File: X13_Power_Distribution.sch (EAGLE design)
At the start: 32 parts

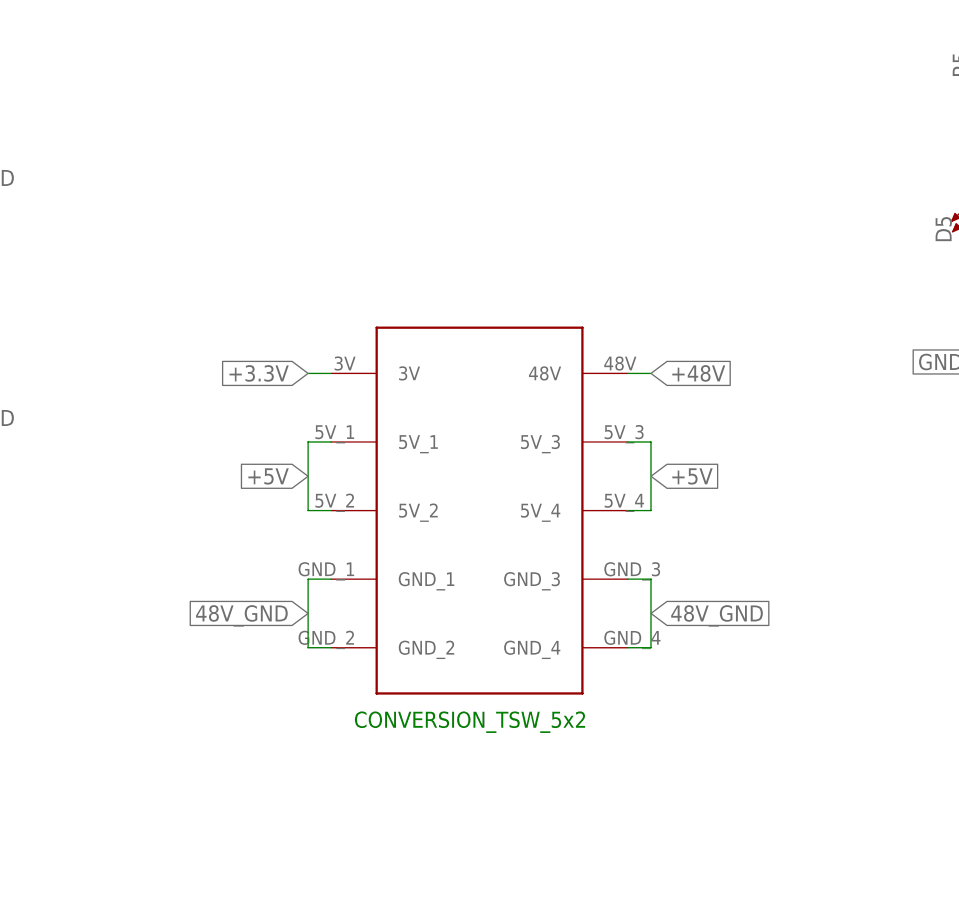
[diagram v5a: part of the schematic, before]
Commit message: removed the custom conversion connector
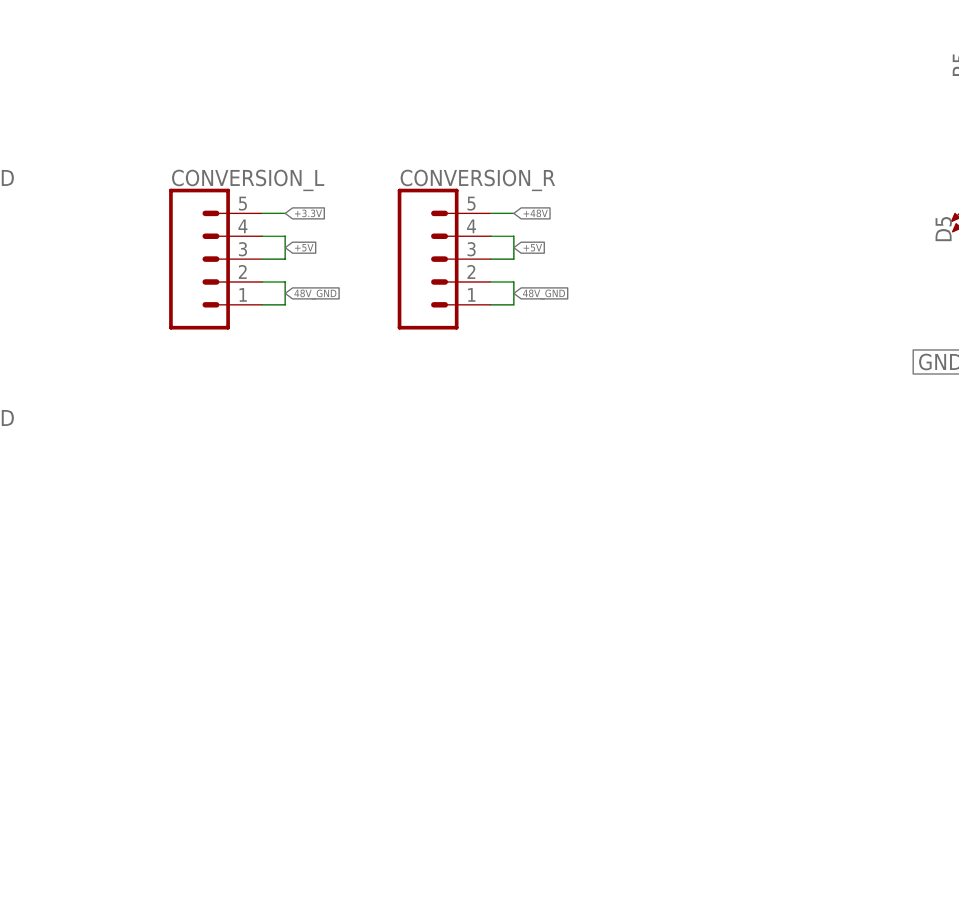
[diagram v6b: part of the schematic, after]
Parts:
- removed U$4: DIST_TO_CONV, Dist_To_Conv_Connector:DIST_TO_CONV
- added CONVERSION_L, CONVERSION_R: (no value), SparkFun-Connectors:CONN_05
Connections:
- net +3.3V: now also CONVERSION_L.5; no longer U$4.3V
- net +48V: now also CONVERSION_R.5; no longer U$4.48V
- net +5V: now also CONVERSION_L.3, CONVERSION_L.4, CONVERSION_R.3, CONVERSION_R.4; no longer U$4.5V_1, U$4.5V_2, U$4.5V_3, U$4.5V_4
- net 48V_GND: now also CONVERSION_L.1, CONVERSION_L.2, CONVERSION_R.1, CONVERSION_R.2; no longer U$4.GND_1, U$4.GND_2, U$4.GND_3, U$4.GND_4
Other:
- note removed: "CONVERSION_TSW_5x2"
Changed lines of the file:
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@@
 <part name="BRICK2_SMBUS" library="SparkFun-Connectors" library_urn="urn:adsk.eagle:library:513" deviceset="CONN_04" device="" package3d_urn="urn:adsk.eagle:package:38085/1"/>
 <part name="BRICK1_SMBUS" library="SparkFun-Connectors" library_urn="urn:adsk.eagle:library:513" deviceset="CONN_04" device="" package3d_urn="urn:adsk.eagle:package:38085/1"/>
-<part name="U$4" library="Dist_To_Conv_Connector" deviceset="DIST_TO_CONV" device=""/>
 <part name="BRICK1_GND" library="SparkFun-Connectors" library_urn="urn:adsk.eagle:library:513" deviceset="CONN_05X2" device="PTH" package3d_urn="urn:adsk.eagle:package:38012/1"/>
 <part name="BRICK1_PWR" library="SparkFun-Connectors" library_urn="urn:adsk.eagle:library:513" deviceset="CONN_05X2" device="PTH" package3d_urn="urn:adsk.eagle:package:38012/1"/>
@@
 <part name="BRICK1_48GND" library="SparkFun-Connectors" library_urn="urn:adsk.eagle:library:513" deviceset="CONN_05X2" device="PTH" package3d_urn="urn:adsk.eagle:package:38012/1"/>
 <part name="BRICK2_48GND" library="SparkFun-Connectors" library_urn="urn:adsk.eagle:library:513" deviceset="CONN_05X2" device="PTH" package3d_urn="urn:adsk.eagle:package:38012/1"/>
+<part name="CONVERSION_L" library="SparkFun-Connectors" library_urn="urn:adsk.eagle:library:513" deviceset="CONN_05" device="" package3d_urn="urn:adsk.eagle:package:38104/1"/>
+<part name="CONVERSION_R" library="SparkFun-Connectors" library_urn="urn:adsk.eagle:library:513" deviceset="CONN_05" device="" package3d_urn="urn:adsk.eagle:package:38104/1"/>
 </parts>
 <sheets>
@@
 <text x="220.98" y="228.6" size="2.54" layer="91">48 VOLT CONNECTOR</text>
 <text x="231.14" y="208.28" size="2.54" layer="91">48 VOLT POE</text>
-<text x="204.47" y="86.36" size="1.778" layer="91">CONVERSION_TSW_5x2</text>
 </plain>
 <instances>
@@
 <attribute name="NAME" x="36.83" y="146.558" size="1.778" layer="95" font="vector"/>
 </instance>
-<instance part="U$4" gate="G$1" x="212.09" y="118.11" smashed="yes"/>
 <instance part="BRICK1_GND" gate="G$1" x="100.33" y="138.43" smashed="yes">
 <attribute name="VALUE" x="96.52" y="128.524" size="1.778" layer="96" font="vector"/>
@@
 <attribute name="VALUE" x="149.86" y="101.854" size="1.778" layer="96" font="vector"/>
 <attribute name="NAME" x="149.86" y="119.888" size="1.778" layer="95" font="vector"/>
+</instance>
+<instance part="CONVERSION_L" gate="G$1" x="186.69" y="138.43" smashed="yes">
+<attribute name="VALUE" x="184.15" y="128.524" size="1.778" layer="96" font="vector"/>
+<attribute name="NAME" x="184.15" y="146.558" size="1.778" layer="95" font="vector"/>
+</instance>
+<instance part="CONVERSION_R" gate="G$1" x="212.09" y="138.43" smashed="yes">
+<attribute name="VALUE" x="209.55" y="128.524" size="1.778" layer="96" font="vector"/>
+<attribute name="NAME" x="209.55" y="146.558" size="1.778" layer="95" font="vector"/>
 </instance>
 </instances>
@@
 </segment>
 <segment>
-<pinref part="U$4" gate="G$1" pin="48V"/>
-<wire x1="234.95" y1="125.73" x2="237.49" y2="125.73" width="0.1524" layer="91"/>
-<label x="237.49" y="125.73" size="1.778" layer="95" xref="yes"/>
-</segment>
-<segment>
 <pinref part="BRICK1_48V" gate="G$1" pin="1"/>
 <wire x1="119.38" y1="143.51" x2="116.84" y2="143.51" width="0.1524" layer="91"/>
@@
 <label x="116.84" y="106.68" size="0.8128" layer="95" rot="R270" xref="yes"/>
 </segment>
+<segment>
+<pinref part="CONVERSION_R" gate="G$1" pin="5"/>
+<wire x1="222.25" y1="143.51" x2="219.71" y2="143.51" width="0.1524" layer="91"/>
+<label x="222.25" y="143.51" size="0.8128" layer="95" xref="yes"/>
+</segment>
 </net>
 <net name="48V_GND" class="0">
@@
 <wire x1="251.46" y1="198.12" x2="241.3" y2="198.12" width="0.1524" layer="91"/>
 <label x="241.3" y="198.12" size="1.778" layer="95" rot="R180" xref="yes"/>
-</segment>
-<segment>
-<pinref part="U$4" gate="G$1" pin="GND_1"/>
-<wire x1="201.93" y1="102.87" x2="199.39" y2="102.87" width="0.1524" layer="91"/>
-<pinref part="U$4" gate="G$1" pin="GND_2"/>
-<wire x1="199.39" y1="102.87" x2="199.39" y2="95.25" width="0.1524" layer="91"/>
-<wire x1="199.39" y1="95.25" x2="201.93" y2="95.25" width="0.1524" layer="91"/>
-<label x="199.39" y="99.06" size="1.778" layer="95" rot="R180" xref="yes"/>
-</segment>
-<segment>
-<pinref part="U$4" gate="G$1" pin="GND_3"/>
-<wire x1="234.95" y1="102.87" x2="237.49" y2="102.87" width="0.1524" layer="91"/>
-<wire x1="237.49" y1="102.87" x2="237.49" y2="95.25" width="0.1524" layer="91"/>
-<pinref part="U$4" gate="G$1" pin="GND_4"/>
-<wire x1="237.49" y1="95.25" x2="234.95" y2="95.25" width="0.1524" layer="91"/>
-<label x="237.49" y="99.06" size="1.778" layer="95" xref="yes"/>
 </segment>
 <segment>
@@
 <label x="143.51" y="106.68" size="0.8128" layer="95" rot="R270" xref="yes"/>
 </segment>
+<segment>
+<pinref part="CONVERSION_L" gate="G$1" pin="2"/>
+<wire x1="196.85" y1="135.89" x2="194.31" y2="135.89" width="0.1524" layer="91"/>
+<pinref part="CONVERSION_L" gate="G$1" pin="1"/>
+<wire x1="196.85" y1="133.35" x2="194.31" y2="133.35" width="0.1524" layer="91"/>
+<wire x1="196.85" y1="135.89" x2="196.85" y2="133.35" width="0.1524" layer="91"/>
+<label x="196.85" y="134.62" size="0.8128" layer="95" xref="yes"/>
+</segment>
+<segment>
+<pinref part="CONVERSION_R" gate="G$1" pin="2"/>
+<wire x1="222.25" y1="135.89" x2="219.71" y2="135.89" width="0.1524" layer="91"/>
+<pinref part="CONVERSION_R" gate="G$1" pin="1"/>
+<wire x1="222.25" y1="133.35" x2="219.71" y2="133.35" width="0.1524" layer="91"/>
+<wire x1="222.25" y1="135.89" x2="222.25" y2="133.35" width="0.1524" layer="91"/>
+<label x="222.25" y="134.62" size="0.8128" layer="95" xref="yes"/>
+</segment>
 </net>
 <net name="N$3" class="0">
@@
 </net>
 <net name="+5V" class="0">
-<segment>
-<pinref part="U$4" gate="G$1" pin="5V_2"/>
-<wire x1="201.93" y1="110.49" x2="199.39" y2="110.49" width="0.1524" layer="91"/>
-<wire x1="199.39" y1="110.49" x2="199.39" y2="118.11" width="0.1524" layer="91"/>
-<pinref part="U$4" gate="G$1" pin="5V_1"/>
-<wire x1="199.39" y1="118.11" x2="201.93" y2="118.11" width="0.1524" layer="91"/>
-<label x="199.39" y="114.3" size="1.778" layer="95" rot="R180" xref="yes"/>
-</segment>
-<segment>
-<pinref part="U$4" gate="G$1" pin="5V_3"/>
-<wire x1="234.95" y1="118.11" x2="237.49" y2="118.11" width="0.1524" layer="91"/>
-<wire x1="237.49" y1="118.11" x2="237.49" y2="110.49" width="0.1524" layer="91"/>
-<pinref part="U$4" gate="G$1" pin="5V_4"/>
-<wire x1="237.49" y1="110.49" x2="234.95" y2="110.49" width="0.1524" layer="91"/>
-<label x="237.49" y="114.3" size="1.778" layer="95" xref="yes"/>
-</segment>
 <segment>
 <pinref part="BACKPLANE_SMBUS" gate="G$1" pin="1"/>
@@
 <wire x1="30.48" y1="86.36" x2="30.48" y2="83.82" width="0.1524" layer="91"/>
 <junction x="30.48" y="86.36"/>
+</segment>
+<segment>
+<pinref part="CONVERSION_L" gate="G$1" pin="4"/>
+<wire x1="196.85" y1="140.97" x2="194.31" y2="140.97" width="0.1524" layer="91"/>
+<pinref part="CONVERSION_L" gate="G$1" pin="3"/>
+<wire x1="196.85" y1="138.43" x2="194.31" y2="138.43" width="0.1524" layer="91"/>
+<wire x1="196.85" y1="138.43" x2="196.85" y2="140.97" width="0.1524" layer="91"/>
+<label x="196.85" y="139.7" size="0.8128" layer="95" xref="yes"/>
+</segment>
+<segment>
+<pinref part="CONVERSION_R" gate="G$1" pin="4"/>
+<wire x1="222.25" y1="140.97" x2="219.71" y2="140.97" width="0.1524" layer="91"/>
+<pinref part="CONVERSION_R" gate="G$1" pin="3"/>
+<wire x1="222.25" y1="138.43" x2="219.71" y2="138.43" width="0.1524" layer="91"/>
+<wire x1="222.25" y1="140.97" x2="222.25" y2="138.43" width="0.1524" layer="91"/>
+<label x="222.25" y="139.7" size="0.8128" layer="95" xref="yes"/>
 </segment>
 </net>
@@
 </segment>
 <segment>
-<pinref part="U$4" gate="G$1" pin="3V"/>
-<wire x1="201.93" y1="125.73" x2="199.39" y2="125.73" width="0.1524" layer="91"/>
-<label x="199.39" y="125.73" size="1.778" layer="95" rot="R180" xref="yes"/>
-</segment>
-</net>
+<pinref part="CONVERSION_L" gate="G$1" pin="5"/>
+<wire x1="194.31" y1="143.51" x2="196.85" y2="143.51" width="0.1524" layer="91"/>
+<label x="196.85" y="143.51" size="0.8128" layer="95" xref="yes"/>
+</segment>
+</net>

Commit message: ready for design review 1 :3
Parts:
- removed J1, J2: (no value), SparkFun-Connectors:BANANA_CONN
- added 48V_TETHER: (no value), SparkFun-Connectors:CONN_05X2PTH
- added R4, R6, R7: 1k, SparkFun-Resistors:RESISTOR0603
- BACKPLANE_SMBUS: device SparkFun-Connectors:CONN_04X2 -> SparkFun-Connectors:CONN_05X2PTH
- BRICK1_SMBUS, BRICK2_SMBUS: device SparkFun-Connectors:CONN_04 -> SparkFun-Connectors:CONN_05
- renumbered BRICK1_48GND to BRICK1_VIN(-), BRICK1_48V to BRICK1_VIN(+), BRICK1_GND to BRICK1_VOUT(-), BRICK1_PWR to BRICK1_VOUT(+), BRICK2_48GND to BRICK2_VIN(-), BRICK2_48V to BRICK2_VIN(+), BRICK2_GND to BRICK2_VOUT(-), BRICK2_PWR to BRICK2_VOUT(+)
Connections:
- removed net 48_RAW: D6.C
- new net 3.3V: R4.2, R6.2, R7.2
- new net C2/PGOOD: BACKPLANE_SMBUS.8, BRICK1_SMBUS.1, BRICK2_SMBUS.1
- net +3.3V: now also BACKPLANE_SMBUS.10; no longer BACKPLANE_SMBUS.8
- net +48V_RAW: now also 48V_TETHER.1, 48V_TETHER.3, 48V_TETHER.5, 48V_TETHER.7, 48V_TETHER.9, D6.C; no longer J1.1
- net +5V: now also BACKPLANE_SMBUS.9
- net 48V_GND: now also 48V_TETHER.10, 48V_TETHER.2, 48V_TETHER.4, 48V_TETHER.6, 48V_TETHER.8; no longer J2.1
- net ALERT: now also BACKPLANE_SMBUS.4, R6.1; no longer BACKPLANE_SMBUS.2
- net CLK: now also BRICK1_SMBUS.3, BRICK2_SMBUS.3, R7.1; no longer BRICK1_SMBUS.2, BRICK2_SMBUS.2
- net DATA: now also BACKPLANE_SMBUS.2, BRICK1_SMBUS.5, BRICK2_SMBUS.5, R4.1; no longer BACKPLANE_SMBUS.4, BRICK1_SMBUS.3, BRICK2_SMBUS.3
- net ON/OFF: now also BRICK1_SMBUS.2, BRICK2_SMBUS.2; no longer BRICK1_SMBUS.1, BRICK2_SMBUS.1
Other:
- note added: "PULL-UP RESISTORS"
- note removed: "48 VOLT CONNECTOR"
- moved on the sheet: J3, J4
